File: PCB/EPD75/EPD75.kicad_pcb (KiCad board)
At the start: 2 copper layers, 110 x 168 mm, 110 parts, among them J1 Conn_01x26, J10 TF_PUSH, J11 Reset, J12 TC2030-USB-NL-DS, J4 BTN1, J5 USB-C-Socket-V, J7 USB-C-Socket-V, J8 PWR, Q1 BSS138, U3 MD8942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

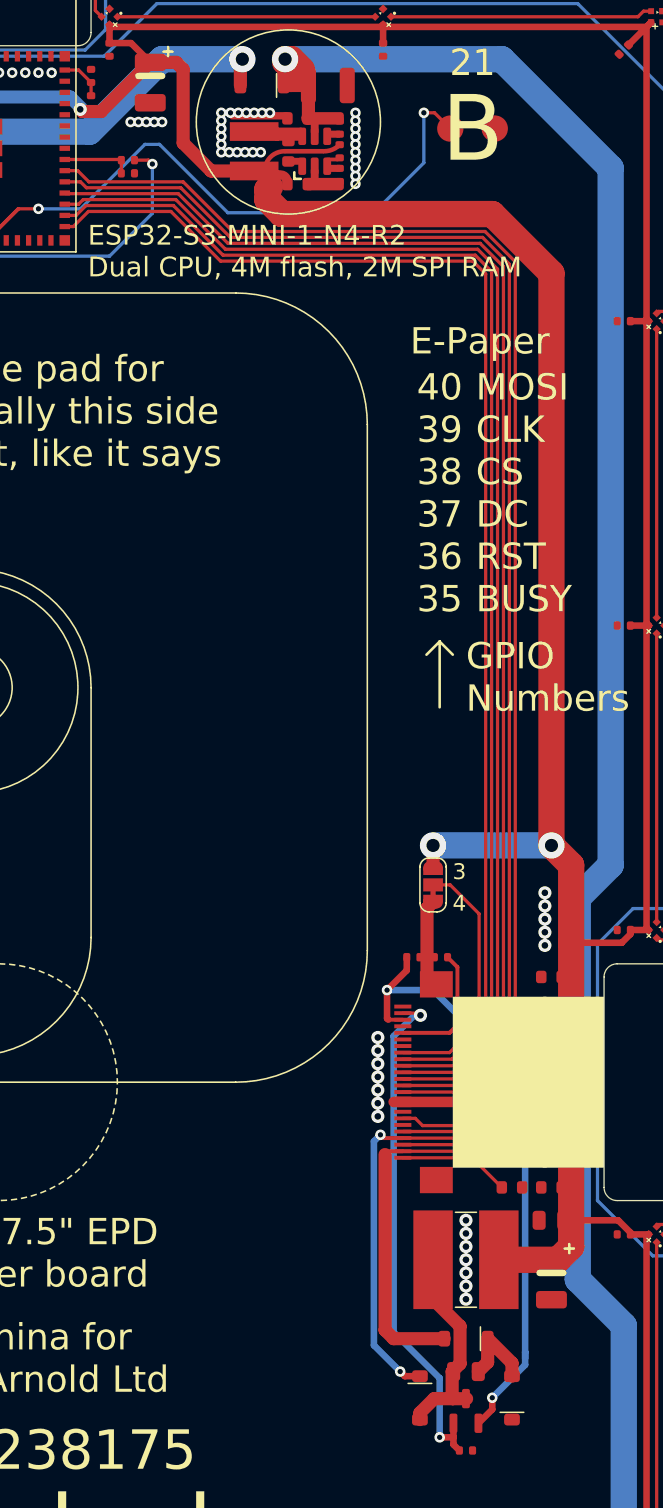
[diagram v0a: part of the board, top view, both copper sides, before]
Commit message: Render and PCB tidy (inductors)
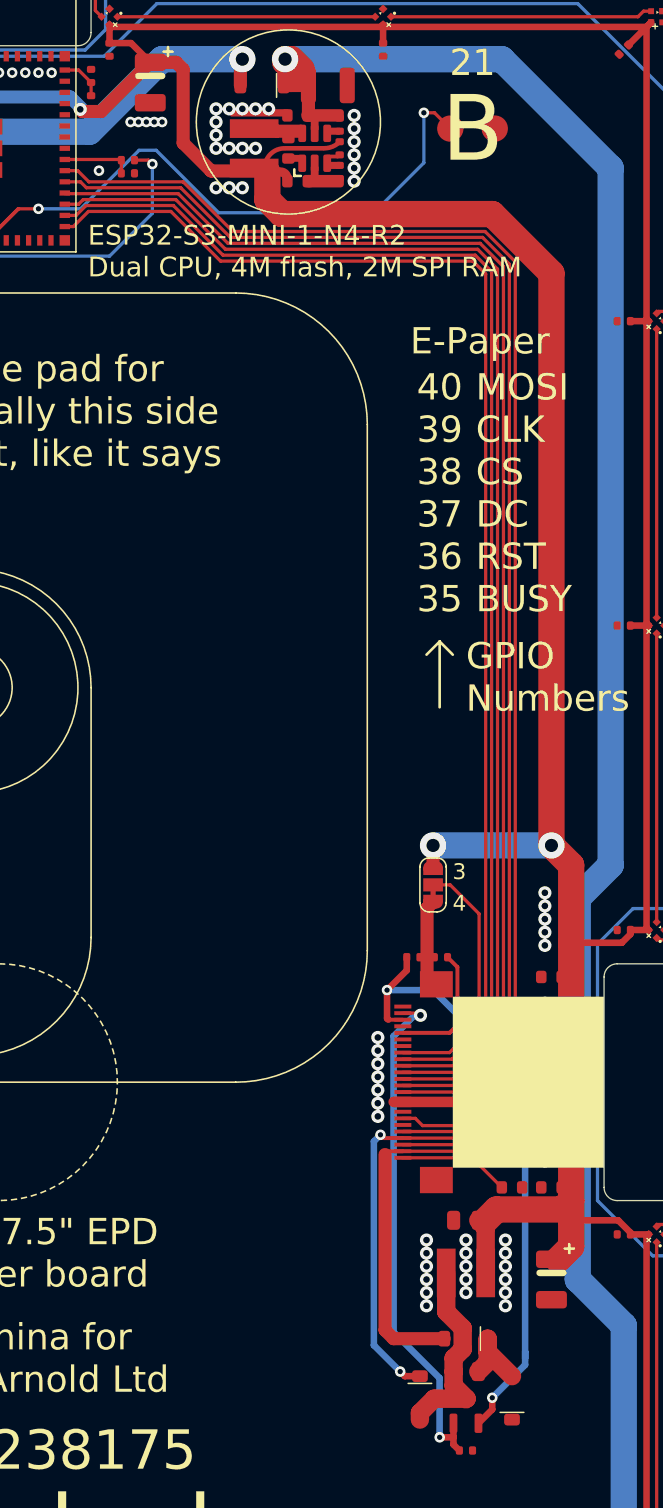
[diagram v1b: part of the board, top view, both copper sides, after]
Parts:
- L1: footprint Inductor_SMD:L_Ferrocore_DLG-0705 -> RevK:L_4x4
- L2: value 10uH -> 47uH 1.3A
- moved C18 6.50 mm to (137.5, 110.5)
- moved L1 1.00 mm to (137.5, 114.5)
- moved C10 0.23 mm to (124.0, 29.0)
- moved C8 0.23 mm to (124.7, 26.5)
- moved C9 0.23 mm to (124.7, 31.5)
- moved L2 0.23 mm to (121.4, 29.0)
- moved R10 0.23 mm to (127.9, 30.9)
- moved R11 0.23 mm to (127.9, 27.2)
- moved R9 0.23 mm to (127.9, 29.0)
- moved U3 0.23 mm to (126.0, 29.0)
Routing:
- net +3.3V: track 824.0 -> 831.9 mm
- net Net-(D3-A): track 13.2 -> 15.3 mm
- net GND: vias 89 -> 93

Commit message: Library update
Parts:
- L2: value 47uH 1.3A -> 10uH
